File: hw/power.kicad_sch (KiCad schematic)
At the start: 39 parts, among them J1501 pwr+data, U1501 TPS74612PQWDRBRQ1, U1502 LMR51430, U1503 TPS22918DBVR, U1504 TPS7A2033PDBVR, U1505 OPA320AIDBVR

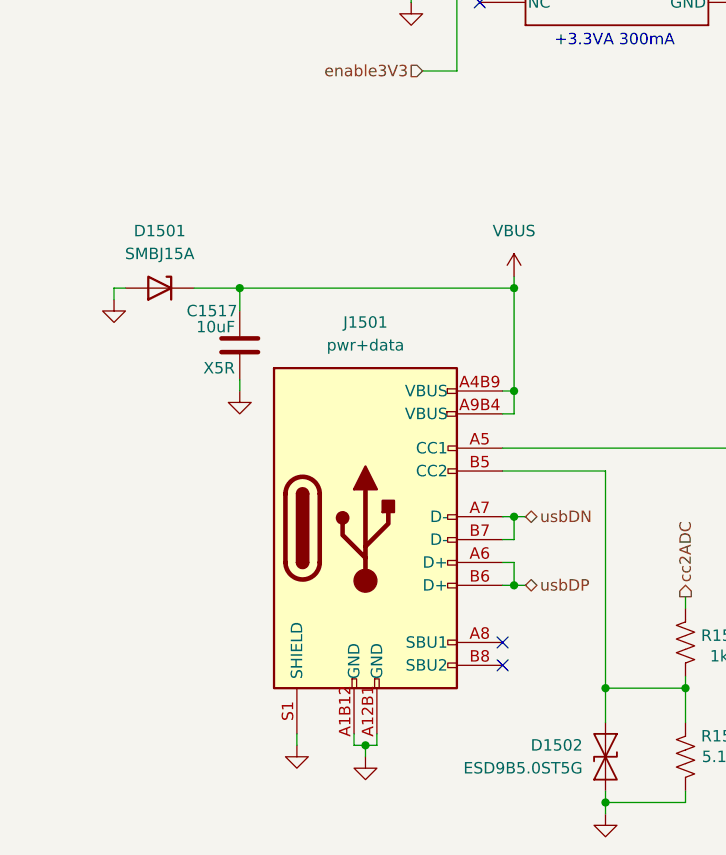
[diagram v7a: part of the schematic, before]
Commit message: Switch to parts I can source from Mouser
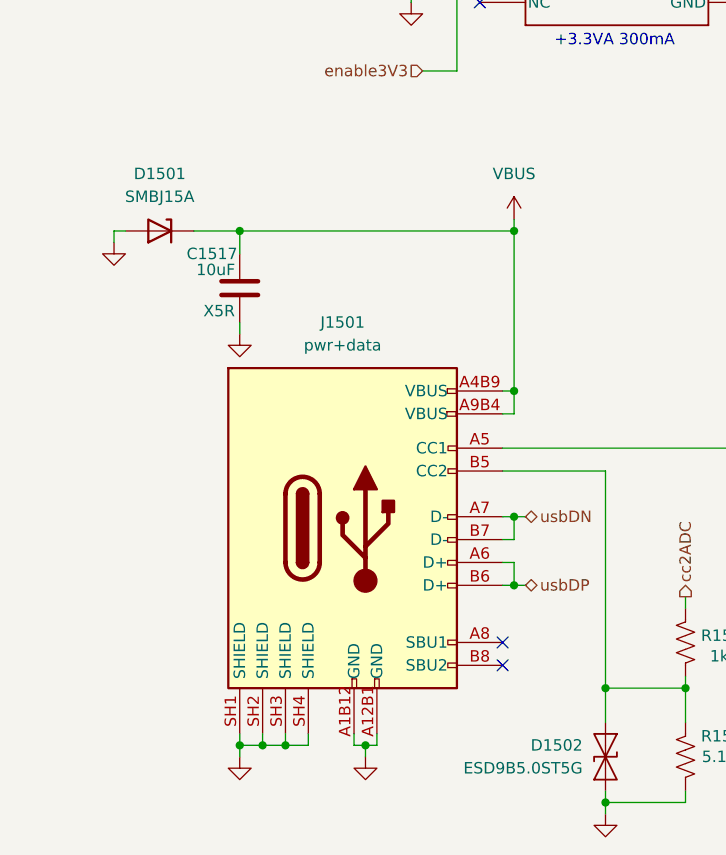
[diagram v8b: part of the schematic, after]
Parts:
- C1501, C1511: MFG (none) -> muRata; MPN (none) -> GCM155R71H104KE02D; Mouser Part Number (none) -> 81-GCM155R71H104KE2D
- C1502, C1506, C1507, C1517: MFG (none) -> Samsung; MPN (none) -> CL10A106MA8NRWC; Mouser Part Number (none) -> 187-CL10A106MA8NRWC
- C1503, C1504, C1505, C1509, C1510: MFG (none) -> muRata; MPN (none) -> GRM155R61E105MA12D; Mouser Part Number (none) -> 81-GRM155R61E105MA2D
- C1508: MFG (none) -> KEMET; MPN (none) -> C0402C301J3GACTU; Mouser Part Number (none) -> 80-C0402C301J3GACTU
- C1512, C1515: MFG (none) -> TAIYO YUDEN; MPN (none) -> TMK105CBJ225MV-F; Mouser Part Number (none) -> 963-TMK105CBJ225MV-F
- C1513, C1514, C1516: MFG (none) -> YAGEO; MPN (none) -> CC0402KRX5R8BB103; Mouser Part Number (none) -> 603-CC0402KRX5R8BB10
- D1501: MFG Littelfuse -> Diotec; MPN SMBJ15A -> 1.0SMBJ15A-AQ; Mouser Part Number (none) -> 637-1.0SMBJ15A-AQ
- D1502, D1503: MFG (none) -> onsemi; MPN (none) -> ESD9B5.0ST5G; Mouser Part Number (none) -> 863-ESD9B5.0ST5G
- FB1501: MFG (none) -> Laird; Mouser Part Number (none) -> 875-MI0603J601R-10
- J1501: footprint Library:USB_C_Receptacle_HRO_TYPE-C-31-M-12-bursted -> Library:AMPHENOL_10155435-00011LF; LCSC_PN C393939 -> (none); MFG (none) -> same sky; MPN TYPE-C-31-M-12 -> UJ20-C-G-MSMT-TR-68; Manufacturer Korean HROparts Elec -> same sky; Mouser Part Number (none) -> 179-UJ20-C-GMSMTTR68
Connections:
- net GND: now also J1501.SH1 (SHIELD), J1501.SH2 (SHIELD), J1501.SH3 (SHIELD), J1501.SH4 (SHIELD); no longer J1501.S1 (SHIELD)
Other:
- moved on the sheet: C1517, D1501
